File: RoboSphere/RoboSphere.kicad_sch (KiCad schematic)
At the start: 15 parts, among them M1 Motor_DC, M2 Motor_DC, M3 Motor_DC, M4 Motor_DC, M5 Motor_DC, M6 Motor_DC, U1 RASPBERRY_PI_ZERO_2_W, U2 4070, U3 4081, U4 DRV8833PW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

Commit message: Kicad H-bridge update
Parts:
- removed C1, C2: C_Polarized_US, symbol Device:C_Polarized_US
- removed M1, M2, M3, M4, M5, M6: Motor_DC, symbol Motor:Motor_DC
- removed R1: R, symbol Device:R
- removed U2, U6: 4070, symbol 4xxx:4070
- removed U3, U5: 4081, symbol 4xxx:4081
- removed U4: DRV8833PW, Package_SO:TSSOP-16_4.4x5mm_P0.65mm, symbol Driver_Motor:DRV8833PW
- added C1: 0.01uF, Capacitor_SMD:C_0805_2012Metric, symbol Device:C
- added C2: 10uF, Capacitor_SMD:C_0805_2012Metric, symbol Device:C
- added C3: 2.2uF, Capacitor_SMD:C_0805_2012Metric, symbol Device:C
- added J2: Conn_01x04_Pin, Connector_PinHeader_2.54mm:PinHeader_1x04_P2.54mm_Vertical, symbol Connector:Conn_01x04_Pin
- added U2: DRV8833PWP, Package_SO:HTSSOP-16-1EP_4.4x5mm_P0.65mm_EP3.4x5mm_Mask2.46x2.31mm_ThermalVias, symbol Driver_Motor:DRV8833PWP
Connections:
- net GND: now also C2.2, C3.2, U2.13 (GND), U2.17 (GND), U2.3 (AISEN), U2.6 (BISEN)
- net at U1.29 (GPIO5): now also U2.16 (AIN1)
- net at U1.3 (GPIO2/SDA1): now also U2.10 (BIN2)
- net at U1.33 (GPIO13): now also U2.1 (~{SLEEP})
- net at U1.5 (GPIO3/SCL): now also U2.9 (BIN1)
- net at U1.7 (GPIO4/GPIO_GCLK): now also U2.15 (AIN2)
- net at U1.8 (GPIO14/TXD0): now also U2.8 (~{FAULT})
- new net: C1.2, U2.11 (VCP)
- new net: C3.1, U2.14 (VINT)
- new net +6V: C1.1, C2.1, U2.12 (VM)
- new net AOUT1: J2.4 (Pin_4), U2.2 (AOUT1)
- new net AOUT2: J2.3 (Pin_3), U2.4 (AOUT2)
- new net BOUT1: J2.2 (Pin_2), U2.7 (BOUT1)
- new net BOUT2: J2.1 (Pin_1), U2.5 (BOUT2)
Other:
- title: (none) -> RoboSphere Driver
- moved on the sheet: U1

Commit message: Power Converter Module
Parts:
- removed J2: Conn_01x04_Pin, Connector_PinHeader_2.54mm:PinHeader_1x04_P2.54mm_Vertical, symbol Connector:Conn_01x04_Pin
- added 10uF, 22uF: C, symbol Device:C
- added 2Ohm1, 8Ohm1, R1: R, symbol Device:R
- added 3350mAh2, 3350mAh3: 3.6V, Battery:BatteryHolder_Keystone_1042_1x18650, symbol Device:Battery_Cell
- added AOUT1, AOUT2, BOUT1, BOUT2: Conn_01x03_Pin, Connector_PinHeader_2.54mm:PinHeader_1x03_P2.54mm_Vertical_SMD_Pin1Left, symbol Connector:Conn_01x03_Pin
- added BAR1: HDSP-4832_2, Display:HDSP-4832, symbol LED:HDSP-4832_2
- added SW1: SW_Push, symbol Switch:SW_Push
- added U3: MIC29302AWD, Package_TO_SOT_SMD:TO-252-5_TabPin3, symbol Regulator_Linear:MIC29302AWD
- added U4: LM3914V, Package_LCC:PLCC-20, symbol Driver_LED:LM3914V
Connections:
- net +5V is gone; now on net +6V: U1.2 (5V_2), U1.4 (5V_4)
- net +6V: now also 22uF.2, 8Ohm1.2, R1.2, U3.4 (VOUT)
- net AOUT1: now also AOUT1.1 (Pin_1), AOUT1.2 (Pin_2), AOUT1.3 (Pin_3)
- net AOUT2: now also AOUT2.1 (Pin_1), AOUT2.2 (Pin_2), AOUT2.3 (Pin_3)
- net BOUT1: now also BOUT1.1 (Pin_1), BOUT1.2 (Pin_2), BOUT1.3 (Pin_3)
- net BOUT2: now also BOUT2.1 (Pin_1), BOUT2.2 (Pin_2), BOUT2.3 (Pin_3)
- net GND: now also 10uF.1, 22uF.1, 2Ohm1.2, 3350mAh2.2 (-), R1.1, U3.3 (GND)
- new net: 3350mAh2.1 (+), 3350mAh3.2 (-)
- new net: 3350mAh3.1 (+), SW1.1
- new net: 10uF.2, SW1.2, U3.1 (EN), U3.2 (VIN)
- new net: 2Ohm1.1, 8Ohm1.1, U3.5 (ADJ)

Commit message: Power % module
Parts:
- renumbered 10uF to 10uF1, 22uF to 22uF1
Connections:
- net GND: now also U4.2 (V-), U4.4 (RLO)
- net at 10uF1.2, SW1.2, U3.1 (EN)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: now also BAR1.1 (A), BAR1.10 (A), BAR1.2 (A), BAR1.3 (A), BAR1.4 (A), BAR1.5 (A), BAR1.6 (A), BAR1.7 (A), BAR1.8 (A), BAR1.9 (A), U4.11 (MODE), U4.3 (V+)
- net at BAR1.11 (K): now also U4.1 (LED1)
- net at BAR1.12 (K): now also U4.20 (LED2)
- net at BAR1.13 (K): now also U4.19 (LED3)
- net at BAR1.14 (K): now also U4.18 (LED4)
- net at BAR1.15 (K): now also U4.17 (LED5)
- net at BAR1.16 (K): now also U4.16 (LED6)
- net at BAR1.17 (K): now also U4.15 (LED7)
- net at BAR1.18 (K): now also U4.14 (LED8)
- net at BAR1.19 (K): now also U4.13 (LED9)
- net at BAR1.20 (K): now also U4.12 (LED10)
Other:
- moved on the sheet: BAR1, U4

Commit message: Setting values
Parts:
- added R2, R3: 1Ω, symbol Device:R
- R1: value R -> 1Ω
- renumbered 2Ohm1 to 2Ω, 8Ohm1 to 8Ω
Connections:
- net +6V: now also R1.1, R2.1, R3.1; no longer R1.2
- net GND: now also R1.2, R2.2, R3.2; no longer R1.1
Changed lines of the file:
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@@
 		(title "RoboSphere Driver")
 	)
-	(text_box "6 Motors\n6V\n500mA\n"
+	(text_box "6 Motors\n6V\n250mA\n"
 		(exclude_from_sim no)
 		(at 193.04 144.78 0)
@@
 	)
 	(junction
+		(at 363.22 127)
+		(diameter 0)
+		(color 0 0 0 0)
+	)
+	(junction
 		(at 218.44 143.51)
 		(diameter 0)
@@
 	)
 	(junction
+		(at 355.6 127)
+		(diameter 0)
+		(color 0 0 0 0)
+	)
+	(junction
 		(at 455.93 100.33)
 		(diameter 0)
@@
 	(wire
 		(pts
+			(xy 370.84 127) (xy 363.22 127)
+		)
+		(stroke
+			(width 0)
+			(type default)
+		)
+	)
+	(wire
+		(pts
 			(xy 218.44 153.67) (xy 218.44 151.13)
 		)
@@
 	(wire
 		(pts
-			(xy 345.44 127) (xy 346.71 127)
+			(xy 345.44 127) (xy 355.6 127)
 		)
 		(stroke
@@
 	(wire
 		(pts
+			(xy 363.22 120.65) (xy 363.22 127)
+		)
+		(stroke
+			(width 0)
+			(type default)
+		)
+	)
+	(wire
+		(pts
 			(xy 281.94 176.53) (xy 284.48 176.53)
 		)
@@
 	(wire
 		(pts
+			(xy 355.6 120.65) (xy 355.6 127)
+		)
+		(stroke
+			(width 0)
+			(type default)
+		)
+	)
+	(wire
+		(pts
 			(xy 455.93 90.17) (xy 455.93 92.71)
 		)
@@
 	(wire
 		(pts
+			(xy 363.22 127) (xy 363.22 133.35)
+		)
+		(stroke
+			(width 0)
+			(type default)
+		)
+	)
+	(wire
+		(pts
 			(xy 445.77 90.17) (xy 440.69 90.17)
 		)
@@
 	(wire
 		(pts
+			(xy 355.6 127) (xy 355.6 133.35)
+		)
+		(stroke
+			(width 0)
+			(type default)
+		)
+	)
+	(wire
+		(pts
 			(xy 455.93 97.79) (xy 455.93 100.33)
 		)
@@
 	)
 	(symbol
+		(lib_id "Device:R")
+		(at 359.41 133.35 90)
+		(unit 1)
+		(exclude_from_sim no)
+		(in_bom yes)
+		(on_board yes)
+		(dnp no)
+		(property "Reference" "R2"
+			(at 359.156 136.652 90)
+			(effects
+				(font
+					(size 1.27 1.27)
+				)
+			)
+		)
+		(property "Value" "1Ω"
+			(at 359.156 139.192 90)
+			(effects
+				(font
+					(size 1.27 1.27)
+				)
+			)
+		)
+		(property "Footprint" ""
+			(at 359.41 135.128 90)
+			(effects
+				(font
+					(size 1.27 1.27)
+				)
+				(hide yes)
+			)
+		)
+		(property "Datasheet" "~"
+			(at 359.41 133.35 0)
+			(effects
+				(font
+					(size 1.27 1.27)
+				)
+				(hide yes)
+			)
+		)
+		(property "Description" "Resistor"
+			(at 359.41 133.35 0)
+			(effects
+				(font
+					(size 1.27 1.27)
+				)
+				(hide yes)
+			)
+		)
+		(pin "1"
+		)
+		(pin "2"
+		)
+		(instances
+			(project ""
+				(path "/2d0e31d3-0d89-4ad2-98de-9a03349e734c"
+					(reference "R2")
+					(unit 1)
+				)
+			)
+		)
+	)
+	(symbol
 		(lib_id "Regulator_Linear:MIC29302AWD")
 		(at 492.76 78.74 0)
@@
 	)
 	(symbol
+		(lib_id "Device:R")
+		(at 359.41 127 90)
+		(unit 1)
+		(exclude_from_sim no)
+		(in_bom yes)
+		(on_board yes)
+		(dnp no)
+		(property "Reference" "R3"
+			(at 359.41 124.714 90)
+			(effects
+				(font
+					(size 1.27 1.27)
+				)
+			)
+		)
+		(property "Value" "1Ω"
+			(at 359.41 129.286 90)
+			(effects
+				(font
+					(size 1.27 1.27)
+				)
+			)
+		)
+		(property "Footprint" ""
+			(at 359.41 128.778 90)
+			(effects
+				(font
+					(size 1.27 1.27)
+				)
+				(hide yes)
+			)
+		)
+		(property "Datasheet" "~"
+			(at 359.41 127 0)
+			(effects
+				(font
+					(size 1.27 1.27)
+				)
+				(hide yes)
+			)
+		)
+		(property "Description" "Resistor"
+			(at 359.41 127 0)
+			(effects
+				(font
+					(size 1.27 1.27)
+				)
+				(hide yes)
+			)
+		)
+		(pin "2"
+		)
+		(pin "1"
+		)
+		(instances
+			(project ""
+				(path "/2d0e31d3-0d89-4ad2-98de-9a03349e734c"
+					(reference "R3")
+					(unit 1)
+				)
+			)
+		)
+	)
+	(symbol
 		(lib_id "Device:C")
 		(at 252.73 184.15 90)
@@
 	(symbol
 		(lib_id "Device:R")
+		(at 359.41 120.65 90)
+		(unit 1)
+		(exclude_from_sim no)
+		(in_bom yes)
+		(on_board yes)
+		(dnp no)
+		(property "Reference" "R1"
+			(at 359.41 114.3 90)
+			(effects
+				(font
+					(size 1.27 1.27)
+				)
+			)
+		)
+		(property "Value" "1Ω"
+			(at 359.41 116.84 90)
+			(effects
+				(font
+					(size 1.27 1.27)
+				)
+			)
+		)
+		(property "Footprint" ""
+			(at 359.41 122.428 90)
+			(effects
+				(font
+					(size 1.27 1.27)
+				)
+				(hide yes)
+			)
+		)
+		(property "Datasheet" "~"
+			(at 359.41 120.65 0)
+			(effects
+				(font
+					(size 1.27 1.27)
+				)
+				(hide yes)
+			)
+		)
+		(property "Description" "Resistor"
+			(at 359.41 120.65 0)
+			(effects
+				(font
+					(size 1.27 1.27)
+				)
+				(hide yes)
+			)
+		)
+		(pin "1"
+		)
+		(pin "2"
+		)
+		(instances
+			(project ""
+				(path "/2d0e31d3-0d89-4ad2-98de-9a03349e734c"
+					(reference "R1")
+					(unit 1)
+				)
+			)
+		)
+	)
+	(symbol
+		(lib_id "Device:R")
 		(at 514.35 86.36 90)
 		(unit 1)
@@
 		(on_board yes)
 		(dnp no)
-		(property "Reference" "2Ohm1"
+		(property "Reference" "2Ω"
 			(at 514.604 88.9 90)
 			(effects
@@
 			(project ""
 				(path "/2d0e31d3-0d89-4ad2-98de-9a03349e734c"
-					(reference "2Ohm1")
+					(reference "2Ω")
 					(unit 1)
 				)
@@
 	(symbol
 		(lib_id "power:GND")
-		(at 354.33 127 90)
+		(at 370.84 127 90)
 		(unit 1)
 		(exclude_from_sim no)
@@
 		(fields_autoplaced yes)
 		(property "Reference" "#PWR015"
-			(at 360.68 127 0)
+			(at 377.19 127 0)
 			(effects
 				(font
@@
 		)
 		(property "Value" "GND"
-			(at 358.14 126.9999 90)
+			(at 374.65 126.9999 90)
 			(effects
 				(font
@@
 		)
 		(property "Footprint" ""
-			(at 354.33 127 0)
+			(at 370.84 127 0)
 			(effects
 				(font
@@
 		)
 		(property "Datasheet" ""
-			(at 354.33 127 0)
+			(at 370.84 127 0)
 			(effects
 				(font
@@
 		)
 		(property "Description" "Power symbol creates a global label with name \"GND\" , ground"
-			(at 354.33 127 0)
+			(at 370.84 127 0)
 			(effects
 				(font
@@
 		(on_board yes)
 		(dnp no)
-		(property "Reference" "8Ohm1"
-			(at 515.112 80.01 0)
+		(property "Reference" "8Ω"
+			(at 513.334 80.01 0)
 			(effects
 				(font
@@
 			(project ""
 				(path "/2d0e31d3-0d89-4ad2-98de-9a03349e734c"
-					(reference "8Ohm1")
+					(reference "8Ω")
 					(unit 1)
 				)
@@
 					(unit 1)
 				)
-			)
-		)
-	)
-	(symbol
-		(lib_id "Device:R")
-		(at 350.52 127 270)
-		(unit 1)
-		(exclude_from_sim no)
-		(in_bom yes)
-		(on_board yes)
-		(dnp no)
-		(property "Reference" "R1"
-			(at 350.52 124.206 90)
-			(effects
-				(font
-					(size 1.27 1.27)
-				)
-			)
-		)
-		(property "Value" "R"
-			(at 350.52 123.19 0)
-			(effects
-				(font
-					(size 1.27 1.27)
-				)
-				(hide yes)
-			)
-		)
-		(property "Footprint" ""
-			(at 350.52 125.222 90)
-			(effects
-				(font
-					(size 1.27 1.27)
-				)
-				(hide yes)
-			)
-		)
-		(property "Datasheet" "~"
-			(at 350.52 127 0)
-			(effects
-				(font
-					(size 1.27 1.27)
-				)
-				(hide yes)
-			)
-		)
-		(property "Description" "Resistor"
-			(at 350.52 127 0)
-			(effects
-				(font
-					(size 1.27 1.27)
-				)
-				(hide yes)
-			)
-		)
-		(pin "1"
-		)
-		(pin "2"
-		)
-		(instances
-			(project ""
-				(path "/2d0e31d3-0d89-4ad2-98de-9a03349e734c"
-					(reference "R1")
-					(unit 1)
-				)

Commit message: Power Management Updates
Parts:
- removed 22uF1: C, symbol Device:C
- removed 2Ω, 8Ω: R, symbol Device:R
- removed U3: MIC29302AWD, Package_TO_SOT_SMD:TO-252-5_TabPin3, symbol Regulator_Linear:MIC29302AWD
- added U5: L7906, symbol Regulator_Linear:L7905
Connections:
- net +6V: now also U5.2 (VI)
- net GND: now also U5.1 (GND)
- net at 10uF1.2, BAR1.1 (A), BAR1.10 (A)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: now also U5.3 (VO)

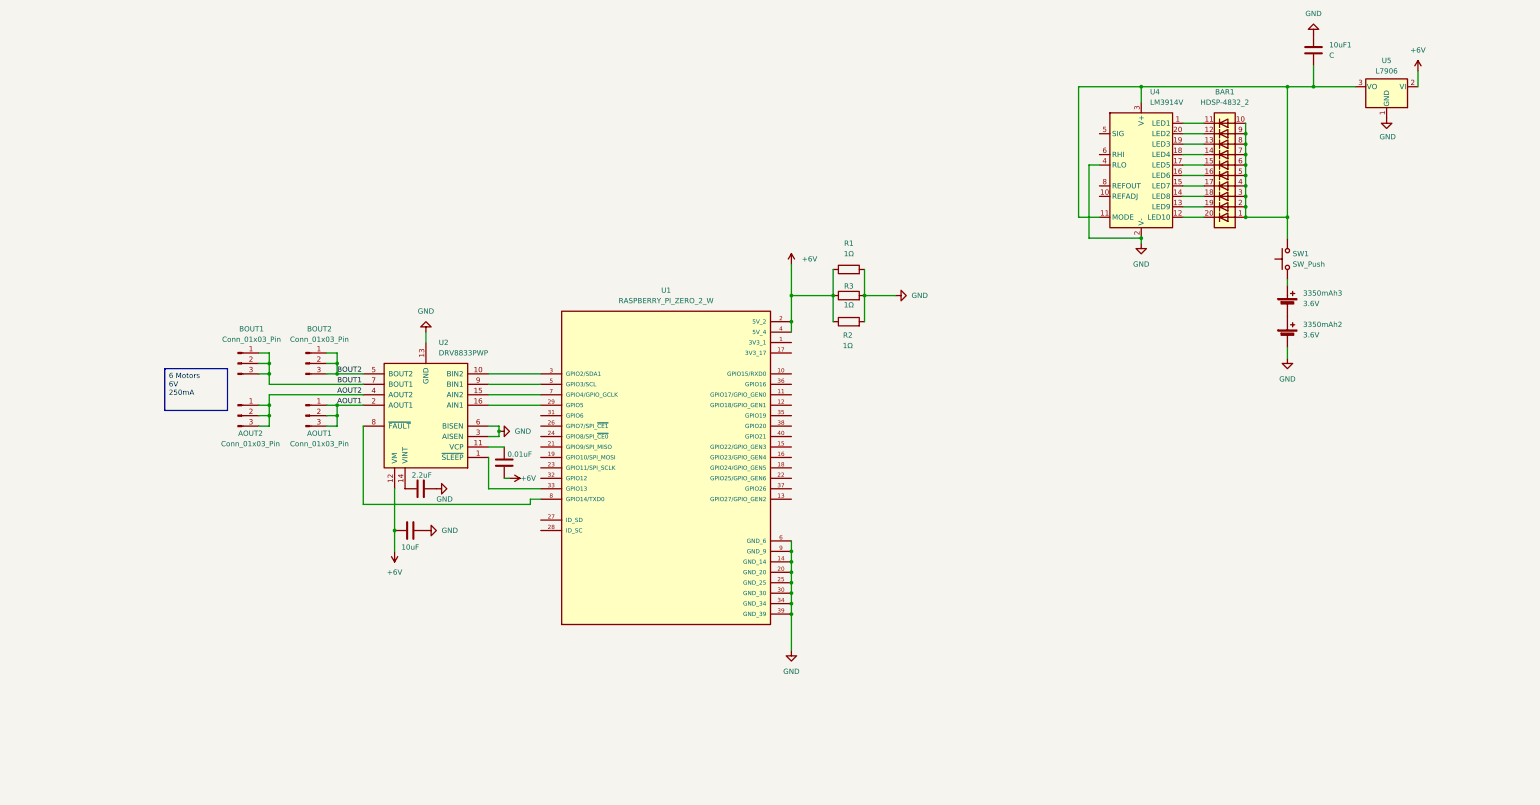
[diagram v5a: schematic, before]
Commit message: Power module update & ADC
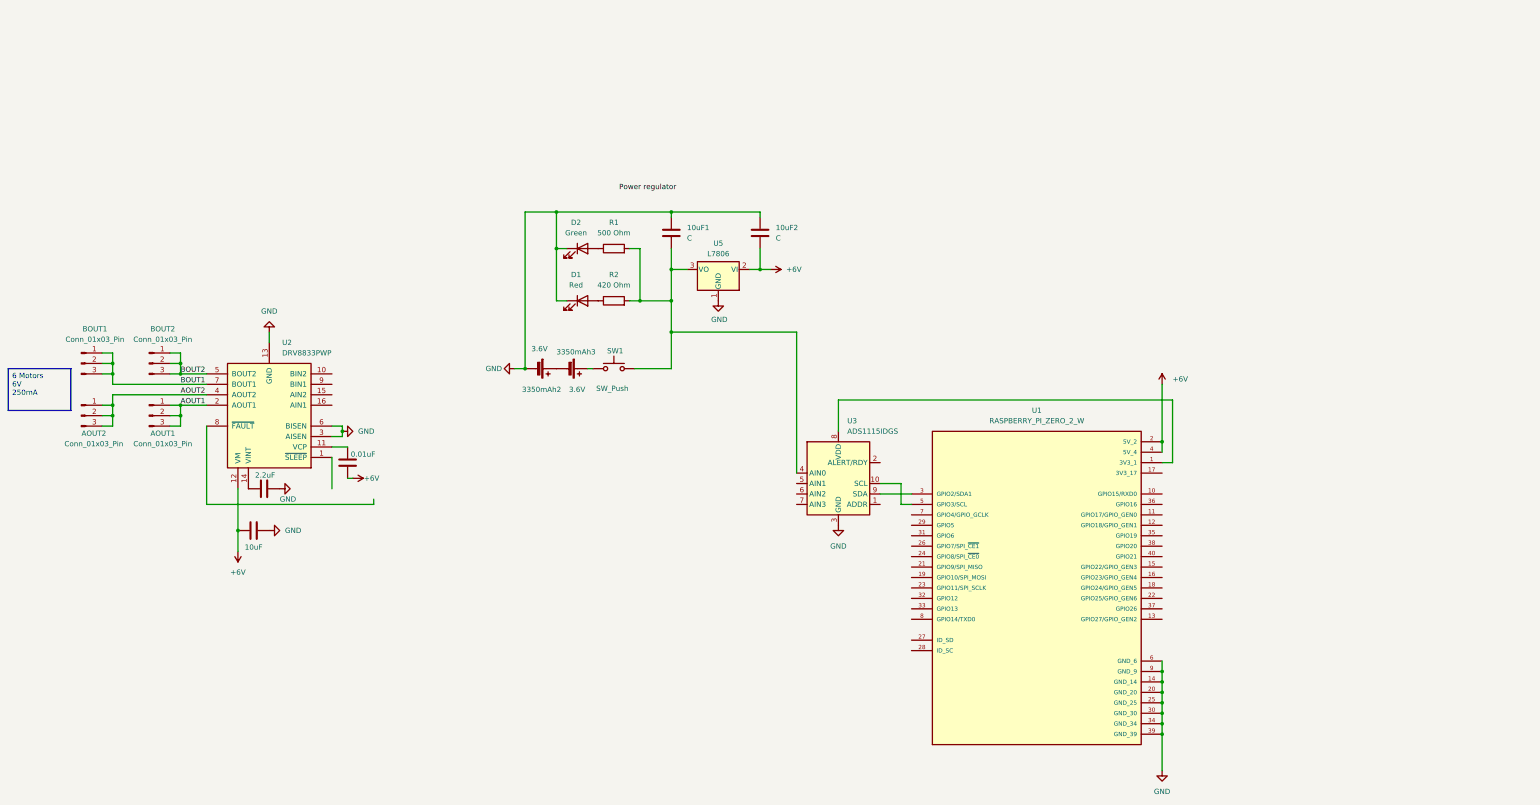
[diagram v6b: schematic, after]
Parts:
- removed BAR1: HDSP-4832_2, Display:HDSP-4832, symbol LED:HDSP-4832_2
- removed R3: 1Ω, symbol Device:R
- removed U4: LM3914V, Package_LCC:PLCC-20, symbol Driver_LED:LM3914V
- added 10uF2: C, symbol Device:C
- added D1: Red, symbol Device:LED
- added D2: Green, symbol Device:LED
- added U3: ADS1115IDGS, Package_SO:TSSOP-10_3x3mm_P0.5mm, symbol Analog_ADC:ADS1115IDGS
- R1: value 1Ω -> 500 Ohm
- R2: value 1Ω -> 420 Ohm
- U5: value L7906 -> L7806
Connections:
- net +6V: now also 10uF2.2; no longer R1.1, R2.1
- net GND: now also 10uF2.1, D1.1 (K), D2.1 (K), U3.3 (GND); no longer R1.2, R2.2
- net at U1.1 (3V3_1): now also U3.8 (VDD)
- net at U1.29 (GPIO5): no longer U2.16 (AIN1)
- net at U1.3 (GPIO2/SDA1): now also U3.9 (SDA); no longer U2.10 (BIN2)
- net at U1.33 (GPIO13): no longer U2.1 (~{SLEEP})
- net at U1.5 (GPIO3/SCL): now also U3.10 (SCL); no longer U2.9 (BIN1)
- net at U1.7 (GPIO4/GPIO_GCLK): no longer U2.15 (AIN2)
- net at U1.8 (GPIO14/TXD0): no longer U2.8 (~{FAULT})
- net at 10uF1.2, SW1.2, U5.3 (VO): now also R1.2, R2.2, U3.4 (AIN0)
- new net: D1.2 (A), R2.1
- new net: D2.2 (A), R1.1
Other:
- moved on the sheet: 10uF1, 3350mAh2, 3350mAh3, AOUT1, AOUT2, BOUT1, BOUT2, SW1, U1, U2, U5

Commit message: Update
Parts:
- removed AOUT1, AOUT2, BOUT1, BOUT2: Conn_01x03_Pin, Connector_PinHeader_2.54mm:PinHeader_1x03_P2.54mm_Vertical_SMD_Pin1Left, symbol Connector:Conn_01x03_Pin
- removed C1: 0.01uF, Capacitor_SMD:C_0805_2012Metric, symbol Device:C
- removed C2: 10uF, Capacitor_SMD:C_0805_2012Metric, symbol Device:C
- removed C3: 2.2uF, Capacitor_SMD:C_0805_2012Metric, symbol Device:C
- removed D1: Red, symbol Device:LED
- removed D2: Green, symbol Device:LED
- removed R2: 420 Ohm, symbol Device:R
- removed U2: DRV8833PWP, Package_SO:HTSSOP-16-1EP_4.4x5mm_P0.65mm_EP3.4x5mm_Mask2.46x2.31mm_ThermalVias, symbol Driver_Motor:DRV8833PWP
- added M1, M2: Motor_DC, symbol Motor:Motor_DC
- added Q1, Q2: BC557, Package_TO_SOT_THT:TO-92_Inline, symbol Transistor_BJT:BC557
- 3350mAh2, 3350mAh3: value 3.6V -> 3.7V
- R1: value 500 Ohm -> R
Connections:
- net +6V: no longer U1.2 (5V_2), U1.4 (5V_4)
- net GND: now also R1.1, M1.2 (-), M2.2 (-); no longer U1.14 (GND_14), U1.20 (GND_20), U1.25 (GND_25), U1.30 (GND_30), U1.34 (GND_34), U1.39 (GND_39), U1.9 (GND_9)
- net at U1.1 (3V3_1): no longer U3.8 (VDD)
- net at U1.12 (GPIO18/GPIO_GEN1): now also Q2.2 (B)
- net at U1.29 (GPIO5): now also U3.2 (ALERT/RDY)
- net at U1.32 (GPIO12): now also Q1.2 (B)
- new net: U1.2 (5V_2), U3.8 (VDD)
- new net: Q1.1 (C), Q2.1 (C), U1.4 (5V_4)
- new net: M2.1 (+), Q1.3 (E)
- new net: M1.1 (+), Q2.3 (E)
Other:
- moved on the sheet: 10uF1, 10uF2, 3350mAh2, 3350mAh3, SW1, U5
